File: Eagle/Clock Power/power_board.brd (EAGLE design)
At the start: 16 parts

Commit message: Eagle scheme update
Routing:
- net S$14: track 56.7 -> 52.2 mm
- net S$1: track 12.1 -> 14.6 mm
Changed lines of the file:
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@@
 <layer number="14" name="Route14" color="1" fill="6" visible="no" active="no"/>
 <layer number="15" name="Route15" color="4" fill="6" visible="no" active="no"/>
-<layer number="16" name="Bottom" color="1" fill="1" visible="yes" active="yes"/>
+<layer number="16" name="Bottom" color="1" fill="1" visible="no" active="yes"/>
 <layer number="17" name="Pads" color="2" fill="1" visible="yes" active="yes"/>
-<layer number="18" name="Vias" color="2" fill="1" visible="yes" active="yes"/>
-<layer number="19" name="Unrouted" color="6" fill="1" visible="yes" active="yes"/>
-<layer number="20" name="Dimension" color="15" fill="1" visible="yes" active="yes"/>
-<layer number="21" name="tPlace" color="7" fill="1" visible="yes" active="yes"/>
-<layer number="22" name="bPlace" color="7" fill="1" visible="yes" active="yes"/>
-<layer number="23" name="tOrigins" color="15" fill="1" visible="yes" active="yes"/>
-<layer number="24" name="bOrigins" color="15" fill="1" visible="yes" active="yes"/>
-<layer number="25" name="tNames" color="7" fill="1" visible="yes" active="yes"/>
-<layer number="26" name="bNames" color="7" fill="1" visible="yes" active="yes"/>
-<layer number="27" name="tValues" color="7" fill="1" visible="yes" active="yes"/>
-<layer number="28" name="bValues" color="7" fill="1" visible="yes" active="yes"/>
-<layer number="29" name="tStop" color="7" fill="3" visible="yes" active="yes"/>
-<layer number="30" name="bStop" color="7" fill="6" visible="yes" active="yes"/>
-<layer number="31" name="tCream" color="7" fill="4" visible="yes" active="yes"/>
-<layer number="32" name="bCream" color="7" fill="5" visible="yes" active="yes"/>
-<layer number="33" name="tFinish" color="6" fill="3" visible="yes" active="yes"/>
-<layer number="34" name="bFinish" color="6" fill="6" visible="yes" active="yes"/>
-<layer number="35" name="tGlue" color="7" fill="4" visible="yes" active="yes"/>
-<layer number="36" name="bGlue" color="7" fill="5" visible="yes" active="yes"/>
-<layer number="37" name="tTest" color="7" fill="1" visible="yes" active="yes"/>
-<layer number="38" name="bTest" color="7" fill="1" visible="yes" active="yes"/>
-<layer number="39" name="tKeepout" color="4" fill="11" visible="yes" active="yes"/>
-<layer number="40" name="bKeepout" color="1" fill="11" visible="yes" active="yes"/>
-<layer number="41" name="tRestrict" color="4" fill="10" visible="yes" active="yes"/>
-<layer number="42" name="bRestrict" color="1" fill="10" visible="yes" active="yes"/>
-<layer number="43" name="vRestrict" color="2" fill="10" visible="yes" active="yes"/>
-<layer number="44" name="Drills" color="7" fill="1" visible="yes" active="yes"/>
-<layer number="45" name="Holes" color="7" fill="1" visible="yes" active="yes"/>
-<layer number="46" name="Milling" color="3" fill="1" visible="yes" active="yes"/>
-<layer number="47" name="Measures" color="7" fill="1" visible="yes" active="yes"/>
-<layer number="48" name="Document" color="7" fill="1" visible="yes" active="yes"/>
-<layer number="49" name="Reference" color="7" fill="1" visible="yes" active="yes"/>
-<layer number="51" name="tDocu" color="7" fill="1" visible="yes" active="yes"/>
-<layer number="52" name="bDocu" color="7" fill="1" visible="yes" active="yes"/>
+<layer number="18" name="Vias" color="2" fill="1" visible="no" active="yes"/>
+<layer number="19" name="Unrouted" color="6" fill="1" visible="no" active="yes"/>
+<layer number="20" name="Dimension" color="15" fill="1" visible="no" active="yes"/>
+<layer number="21" name="tPlace" color="7" fill="1" visible="no" active="yes"/>
+<layer number="22" name="bPlace" color="7" fill="1" visible="no" active="yes"/>
+<layer number="23" name="tOrigins" color="15" fill="1" visible="no" active="yes"/>
+<layer number="24" name="bOrigins" color="15" fill="1" visible="no" active="yes"/>
+<layer number="25" name="tNames" color="7" fill="1" visible="no" active="yes"/>
+<layer number="26" name="bNames" color="7" fill="1" visible="no" active="yes"/>
+<layer number="27" name="tValues" color="7" fill="1" visible="no" active="yes"/>
+<layer number="28" name="bValues" color="7" fill="1" visible="no" active="yes"/>
+<layer number="29" name="tStop" color="7" fill="3" visible="no" active="yes"/>
+<layer number="30" name="bStop" color="7" fill="6" visible="no" active="yes"/>
+<layer number="31" name="tCream" color="7" fill="4" visible="no" active="yes"/>
+<layer number="32" name="bCream" color="7" fill="5" visible="no" active="yes"/>
+<layer number="33" name="tFinish" color="6" fill="3" visible="no" active="yes"/>
+<layer number="34" name="bFinish" color="6" fill="6" visible="no" active="yes"/>
+<layer number="35" name="tGlue" color="7" fill="4" visible="no" active="yes"/>
+<layer number="36" name="bGlue" color="7" fill="5" visible="no" active="yes"/>
+<layer number="37" name="tTest" color="7" fill="1" visible="no" active="yes"/>
+<layer number="38" name="bTest" color="7" fill="1" visible="no" active="yes"/>
+<layer number="39" name="tKeepout" color="4" fill="11" visible="no" active="yes"/>
+<layer number="40" name="bKeepout" color="1" fill="11" visible="no" active="yes"/>
+<layer number="41" name="tRestrict" color="4" fill="10" visible="no" active="yes"/>
+<layer number="42" name="bRestrict" color="1" fill="10" visible="no" active="yes"/>
+<layer number="43" name="vRestrict" color="2" fill="10" visible="no" active="yes"/>
+<layer number="44" name="Drills" color="7" fill="1" visible="no" active="yes"/>
+<layer number="45" name="Holes" color="7" fill="1" visible="no" active="yes"/>
+<layer number="46" name="Milling" color="3" fill="1" visible="no" active="yes"/>
+<layer number="47" name="Measures" color="7" fill="1" visible="no" active="yes"/>
+<layer number="48" name="Document" color="7" fill="1" visible="no" active="yes"/>
+<layer number="49" name="Reference" color="7" fill="1" visible="no" active="yes"/>
+<layer number="51" name="tDocu" color="7" fill="1" visible="no" active="yes"/>
+<layer number="52" name="bDocu" color="7" fill="1" visible="no" active="yes"/>
 <layer number="91" name="Nets" color="2" fill="1" visible="no" active="no"/>
 <layer number="92" name="Busses" color="1" fill="1" visible="no" active="no"/>
@@
 <text x="-6.35" y="62.865" size="1.016" layer="1">+5 OUT</text>
 <text x="-6.35" y="60.325" size="1.016" layer="1">GND OUT</text>
-<text x="-6.35" y="47.625" size="1.016" layer="1">+9 BAT</text>
-<text x="-6.35" y="45.085" size="1.016" layer="1">GND BAT</text>
+<text x="-6.35" y="45.085" size="1.016" layer="1">+9 BAT</text>
+<text x="-6.35" y="42.545" size="1.016" layer="1">GND BAT</text>
 <text x="6.985" y="43.18" size="1.016" layer="1">7809</text>
 <text x="16.51" y="43.18" size="1.016" layer="1">7805</text>
@@
 <wire x1="46.99" y1="71.12" x2="53.34" y2="71.12" width="1.6764" layer="1"/>
 <wire x1="53.34" y1="71.12" x2="53.34" y2="54.61" width="1.6764" layer="1"/>
-<wire x1="53.34" y1="54.61" x2="53.34" y2="52.705" width="1.27" layer="1"/>
+<wire x1="53.34" y1="54.61" x2="53.34" y2="52.705" width="1.6764" layer="1"/>
 <wire x1="53.34" y1="54.61" x2="51.435" y2="54.61" width="1.27" layer="1"/>
 </signal>
@@
 </signal>
 <signal name="S$1">
-<wire x1="6.35" y1="57.15" x2="11.43" y2="57.15" width="1.6764" layer="1"/>
-<wire x1="11.43" y1="57.15" x2="11.43" y2="50.8" width="1.6764" layer="1"/>
-<wire x1="11.43" y1="57.15" x2="12.065" y2="57.15" width="1.6764" layer="1"/>
+<wire x1="6.35" y1="57.15" x2="8.89" y2="57.15" width="1.6764" layer="1"/>
+<wire x1="8.89" y1="57.15" x2="8.89" y2="53.34" width="1.6764" layer="1"/>
+<wire x1="8.89" y1="53.34" x2="11.43" y2="53.34" width="1.6764" layer="1"/>
+<wire x1="11.43" y1="53.34" x2="11.43" y2="50.8" width="1.6764" layer="1"/>
+<wire x1="8.89" y1="57.15" x2="12.065" y2="57.15" width="1.6764" layer="1"/>
 </signal>
 <signal name="S$10">
@@
 </signal>
 <signal name="S$14">
-<wire x1="17.145" y1="53.975" x2="25.4" y2="53.975" width="1.27" layer="1"/>
+<wire x1="17.145" y1="53.975" x2="20.955" y2="53.975" width="1.27" layer="1"/>
 <wire x1="38.1" y1="52.07" x2="38.1" y2="50.165" width="1.016" layer="1"/>
-<wire x1="38.1" y1="50.165" x2="25.4" y2="50.165" width="1.016" layer="1"/>
-<wire x1="25.4" y1="50.165" x2="25.4" y2="45.72" width="1.27" layer="1"/>
-<wire x1="25.4" y1="45.72" x2="19.05" y2="45.72" width="1.27" layer="1"/>
-<wire x1="25.4" y1="53.975" x2="25.4" y2="50.165" width="1.27" layer="1"/>
+<wire x1="38.1" y1="50.165" x2="20.955" y2="50.165" width="1.016" layer="1"/>
+<wire x1="20.955" y1="50.165" x2="20.955" y2="45.72" width="1.27" layer="1"/>
+<wire x1="20.955" y1="45.72" x2="19.05" y2="45.72" width="1.27" layer="1"/>
+<wire x1="20.955" y1="53.975" x2="20.955" y2="50.165" width="1.27" layer="1"/>
 <wire x1="6.35" y1="63.5" x2="7.62" y2="63.5" width="1.27" layer="1"/>
 <wire x1="7.62" y1="63.5" x2="7.62" y2="59.69" width="1.27" layer="1"/>

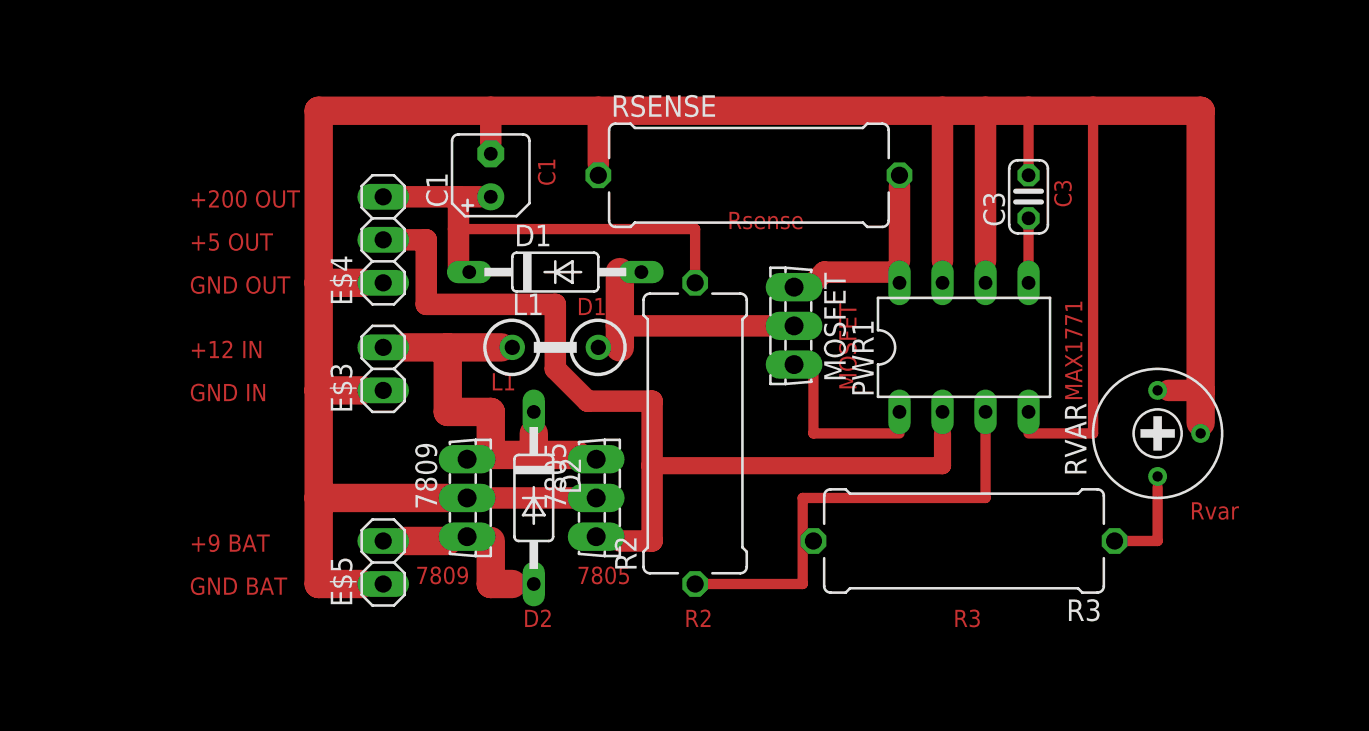
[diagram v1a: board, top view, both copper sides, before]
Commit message: Добавлен диод резервного питания, выключатели питания общий и лампочек отдельно.
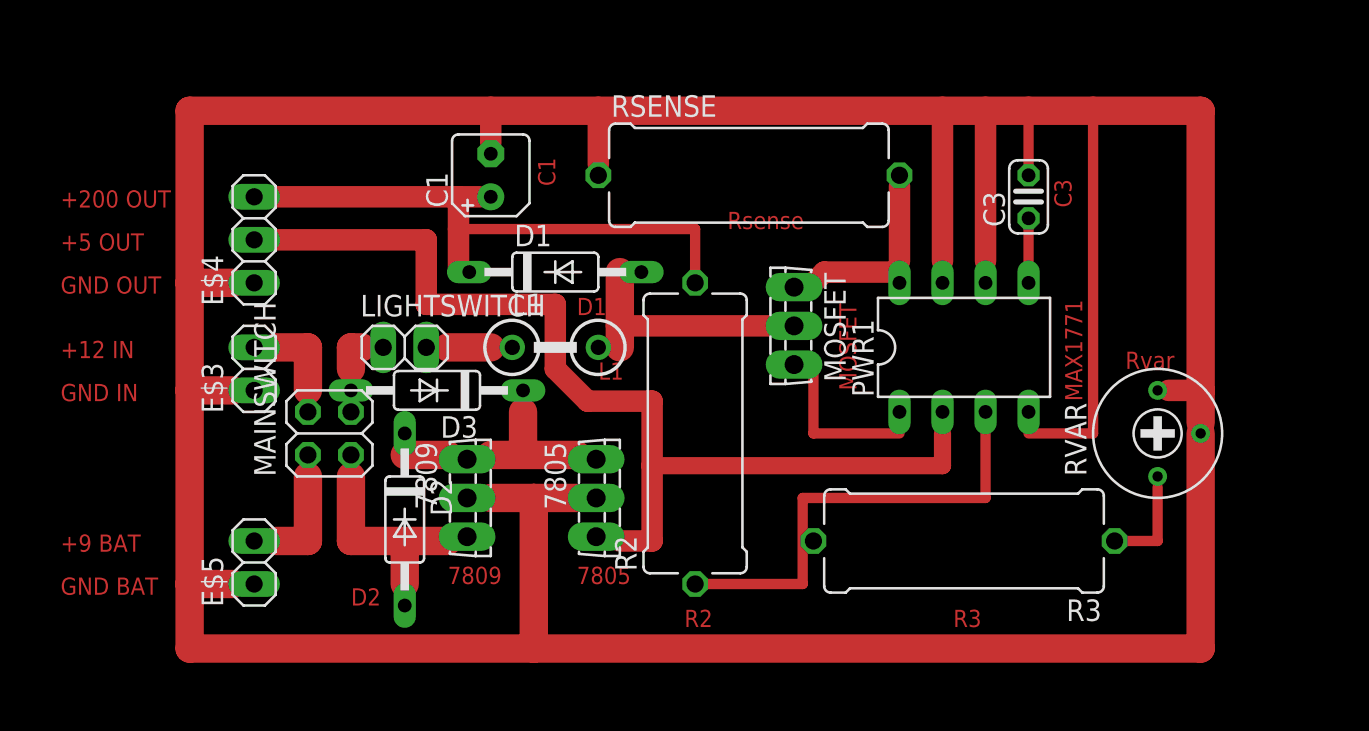
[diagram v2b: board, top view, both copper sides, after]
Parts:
- added D3: (no value), diode:C2992
- added LIGHTSWITCH: (no value), pinhead:1X02
- added MAINSWITCH: (no value), pinhead:2X02
- moved D2 7.73 mm to (6.35, 47.0)
- moved E$3 7.62 mm to (-2.54, 55.9)
- moved E$4 7.62 mm to (-2.54, 63.5)
- moved E$5 7.62 mm to (-2.54, 44.5)
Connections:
- new net GND: RVAR.2
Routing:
- net GND: track 164.5 -> 254.6 mm
- net S$1: track 14.6 -> 1.90 mm
- net S$6: track 2.54 -> 12.1 mm
- net S$8: track 4.45 -> 12.1 mm
- net S$14: track 52.2 -> 59.8 mm
- net MAINSWITCH: track 0.00 -> 5.72 mm
- net S$15: track 0.00 -> 4.44 mm
- net S$7: track 5.08 -> 2.54 mm
- net S$13: track 0.00 -> 1.91 mm
- net S$16: track 6.35 -> 5.08 mm
- net S$17: track 3.81 -> 2.54 mm

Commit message: Eagle Scheme update
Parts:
- added C2, C4: (no value), rcl:C025-024X044
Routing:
- net S$14: track 59.8 -> 64.3 mm
- net GND: track 254.6 -> 257.2 mm
- net S$18: track 0.00 -> 0.64 mm
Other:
- board text added: "D3"
- board text added: "LHT"
- board text added: "PWR"
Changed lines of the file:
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@@
 <plain>
 <text x="45.72" y="65.405" size="1.016" layer="1" rot="R90">C3</text>
-<text x="25.4" y="64.135" size="1.016" layer="1">Rsense</text>
+<text x="25.4" y="62.865" size="1.016" layer="1">Rsense</text>
 <text x="33.02" y="54.61" size="1.016" layer="1" rot="R90">MOSFET</text>
 <text x="46.355" y="53.975" size="1.016" layer="1" rot="R90">MAX1771</text>
@@
 <text x="15.24" y="66.675" size="1.016" layer="1" rot="R90">C1</text>
 <text x="3.175" y="41.91" size="1.016" layer="1">D2</text>
+<text x="7.62" y="52.07" size="1.016" layer="1">D3</text>
+<text x="-1.27" y="49.53" size="1.016" layer="1" rot="R90">PWR</text>
+<text x="5.715" y="60.325" size="1.016" layer="1" rot="R180">LHT</text>
+<rectangle x1="-6.35" y1="67.945" x2="9.525" y2="71.12" layer="1"/>
+<rectangle x1="-6.35" y1="39.37" x2="2.54" y2="41.275" layer="1"/>
+<rectangle x1="-6.35" y1="47.625" x2="-3.175" y2="52.07" layer="1"/>
+<rectangle x1="25.4" y1="39.37" x2="37.465" y2="41.91" layer="1"/>
+<rectangle x1="41.275" y1="39.37" x2="53.34" y2="44.45" layer="1"/>
+<rectangle x1="17.78" y1="68.58" x2="33.655" y2="71.12" layer="1"/>
+<rectangle x1="19.05" y1="65.405" x2="33.655" y2="69.215" layer="1"/>
+<rectangle x1="38.1" y1="61.595" x2="40.64" y2="71.12" layer="1"/>
+<rectangle x1="40.64" y1="67.945" x2="52.705" y2="70.485" layer="1"/>
+<rectangle x1="46.99" y1="57.785" x2="53.34" y2="68.58" layer="1"/>
 </plain>
 <attributes>
@@
 <element name="MAINSWITCH" library="pinhead" package="2X02" value="" x="1.905" y="52.07" rot="R90"/>
 <element name="LIGHTSWITCH" library="pinhead" package="1X02" value="" x="6.35" y="57.15"/>
+<element name="C2" library="rcl" package="C025-024X044" value="" x="17.78" y="41.91" rot="R180"/>
+<element name="C4" library="rcl" package="C025-024X044" value="" x="10.16" y="41.91" rot="R180"/>
 </elements>
 <signals>
@@
 <wire x1="16.51" y1="48.26" x2="13.97" y2="48.26" width="1.6764" layer="1"/>
 <wire x1="13.97" y1="48.26" x2="11.43" y2="48.26" width="1.6764" layer="1"/>
-<wire x1="13.97" y1="39.37" x2="13.97" y2="48.26" width="1.6764" layer="1"/>
+<wire x1="13.97" y1="39.37" x2="13.97" y2="41.91" width="1.6764" layer="1"/>
+<wire x1="13.97" y1="41.91" x2="13.97" y2="48.26" width="1.6764" layer="1"/>
 <wire x1="13.97" y1="39.37" x2="53.34" y2="39.37" width="1.6764" layer="1"/>
 <contactref element="RVAR" pad="2"/>
 <wire x1="53.34" y1="39.37" x2="53.34" y2="52.07" width="1.6764" layer="1"/>
+<wire x1="13.97" y1="41.91" x2="15.24" y2="41.91" width="1.6764" layer="1"/>
+<wire x1="13.97" y1="41.91" x2="12.7" y2="41.91" width="1.6764" layer="1"/>
 </signal>
 <signal name="MAINSWITCH">
@@
 <wire x1="15.24" y1="59.69" x2="15.24" y2="55.88" width="1.27" layer="1"/>
 <wire x1="17.145" y1="53.975" x2="15.24" y2="55.88" width="1.27" layer="1"/>
+<wire x1="20.955" y1="45.72" x2="20.955" y2="41.91" width="1.27" layer="1"/>
+<wire x1="20.955" y1="41.91" x2="20.32" y2="41.91" width="1.27" layer="1"/>
 </signal>
 <signal name="S$16">
@@
 <wire x1="6.35" y1="50.8" x2="8.89" y2="50.8" width="1.6764" layer="1"/>
 </signal>
+<signal name="S$18">
+<wire x1="7.62" y1="41.91" x2="7.62" y2="42.545" width="1.6764" layer="1"/>
+</signal>
 </signals>

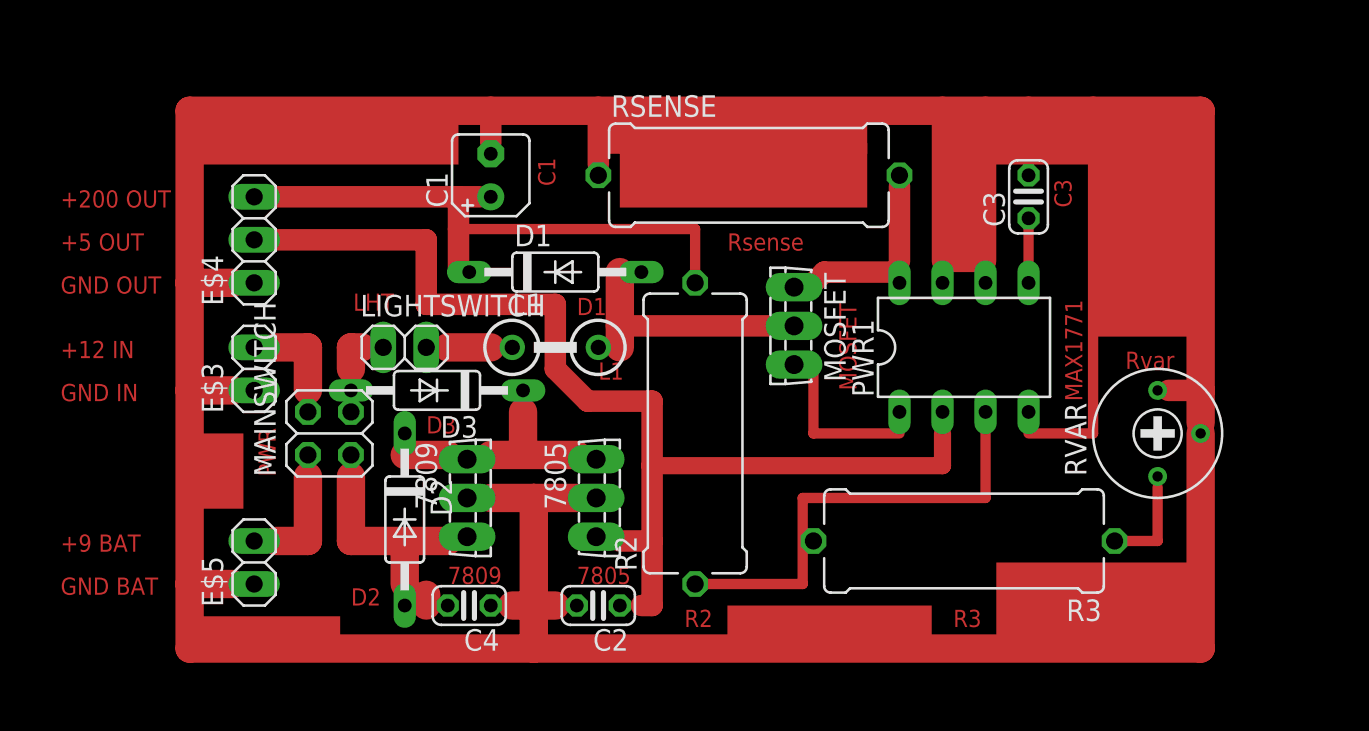
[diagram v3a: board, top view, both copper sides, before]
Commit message: Eagle board changes
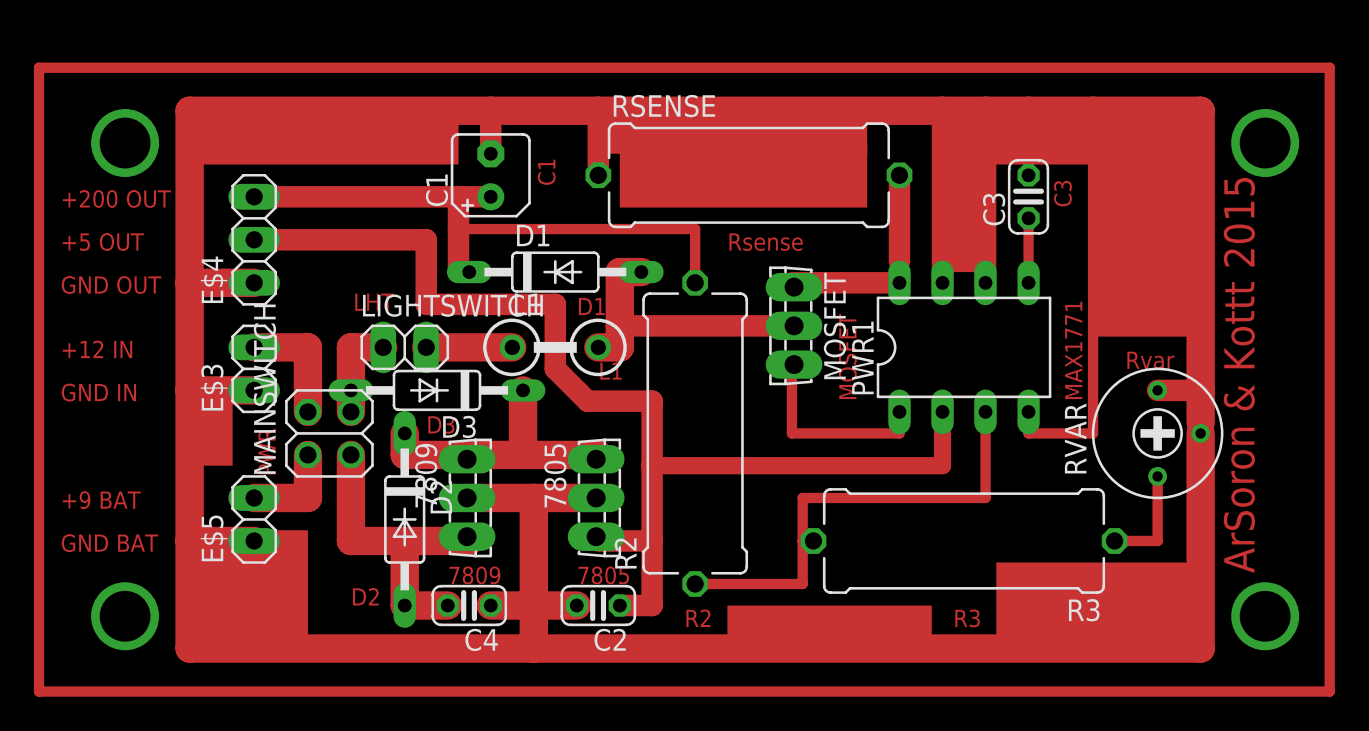
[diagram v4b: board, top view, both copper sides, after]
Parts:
- moved E$5 2.54 mm to (-2.54, 47.0)
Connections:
- new net S$10: D1.A, L1.2
- new net S$11: R3.2
- new net S$5: PWR1.1
- new net S$7: D2.C
- new net S$9: D1.C
- net GND: now also PWR1.4
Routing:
- net S$19: track 0.00 -> 226.1 mm
- net GND: track 257.2 -> 272.4 mm
- net S$14: track 64.3 -> 69.4 mm
- net S$1: track 1.90 -> 5.71 mm
- net S$6: track 12.1 -> 15.9 mm
- net S$10: track 13.3 -> 17.1 mm
- net S$7: track 2.54 -> 5.08 mm
- net S$5: track 8.89 -> 11.4 mm
- net S$11: track 25.4 -> 27.9 mm
- net S$17: track 2.54 -> 5.08 mm
- net S$16: track 5.08 -> 7.62 mm
- net S$15: track 4.44 -> 6.98 mm
- net S$8: track 12.1 -> 14.0 mm
- net S$18: track 0.64 -> 2.54 mm
- net S$2: track 1.91 -> 3.81 mm
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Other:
- board text added: "ArSoron & Kottt 2015"
